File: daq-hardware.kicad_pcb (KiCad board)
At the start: 4 copper layers, 100 x 60 mm, 106 parts, among them J1 USB_B, J10 Screw_Terminal_01x02, J11 Screw_Terminal_01x01, J12 Screw_Terminal_01x01, J13 Screw_Terminal_01x01, J14 Screw_Terminal_01x01, J15 Barrel_Jack_Switch, J2 Micro_SD_Card_Det_Hirose_DM3AT, J3 Conn_01x02, J4 Screw_Terminal_01x02, J5 Screw_Terminal_Thermo_1, J6 Screw_Terminal_Thermo_2, J7 Screw_Terminal_Thermo_3, J8 Screw_Terminal_Thermo_4, J9 Screw_Terminal_01x02, Q1 MMDT2222A, Q2 PMV20ENR, Q3 PMV20ENR, SW1 SW1, SW2 SW1, U1 CP2102N-A01-GQFN24, U10 LTV-817S, U11 ADS131M04, U13 TPS2412PW, U2 ESP32-WROOM-32D, U3 TPS61093, U4 TPS62160DGK, U5 TPS62160DGK, U6 MAX31855RASA, U7 MAX31855RASA, U8 MAX31855RASA, U9 MAX31855RASA

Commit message: Added 3D models, added ptaps sheet, fixed pyros
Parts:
- added D7: CONTINUITY, LED_SMD:LED_0805_2012Metric, F.Cu at (286.4, 116.0)
- added J16: Conn_01x03, Connector_JST:JST_XH_B03B-XH-AM_1x03_P2.50mm_Vertical, F.Cu at (254.9, 117.9)
- added J17: Conn_01x03, Connector_JST:JST_XH_B03B-XH-AM_1x03_P2.50mm_Vertical, F.Cu at (254.9, 125.7)
- added J18: Conn_01x03, Connector_JST:JST_XH_B03B-XH-AM_1x03_P2.50mm_Vertical, F.Cu at (266.8, 117.9)
- added R29: 470, Resistor_SMD:R_0603_1608Metric, F.Cu at (290.6, 115.7)
- added R30: 22k, Resistor_SMD:R_0603_1608Metric, F.Cu at (265.4, 123.5)
- added R31: 43k, Resistor_SMD:R_0603_1608Metric, F.Cu at (277.3, 115.7)
- added R32: 22k, Resistor_SMD:R_0603_1608Metric, F.Cu at (269.4, 123.5)
- added R33: 43k, Resistor_SMD:R_0603_1608Metric, F.Cu at (265.4, 126.0)
- added R34: 22k, Resistor_SMD:R_0603_1608Metric, F.Cu at (277.3, 118.2)
- added R35: 43k, Resistor_SMD:R_0603_1608Metric, F.Cu at (269.4, 126.0)
- D4: value DIODE -> D_Schottky; footprint Diode_SMD:D_SMA -> Diode_SMD:D_SOD-123F
- R2: value 22k1 -> 22k
- R25: value 1k -> 470
- R3: value 47k5 -> 43k
- moved SW1 22.0 mm to (223.0, 152.0)
- moved U11 2.51 mm to (212.6, 52.3)
- moved D4 0.71 mm to (265.8, 87.8), turned to 90 degrees
- turned U10 to 180 degrees
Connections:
- J10 pad 2: Net-(D4-Pad1) -> Net-(D4-Pad2)
- Q2 pad 3: Net-(D4-Pad2) -> Net-(D4-Pad1)
- R25 pad 2: Net-(D4-Pad2) -> Net-(D4-Pad1)
- R26 pad 1: /pyro/CONT -> /CONT
- U10 pad 1: +3V3 -> Net-(D4-Pad2)
- U10 pad 2: /pyro/CONT -> Net-(R27-Pad1)
- U10 pad 3: Net-(R27-Pad1) -> /CONT
- U10 pad 4: Net-(D4-Pad1) -> +3V3
- U2 pad 36: (no net) -> /CONT
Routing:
- net Net-(D4-Pad2): track 17.7 -> 6.17 mm, vias 0 -> 1
- net Net-(D4-Pad1): track 7.27 -> 16.1 mm, vias 1 -> 0
- net +3V3: track 33.8 -> 27.3 mm
- net /pyro/CONT: track 3.93 -> 0.00 mm
- net Net-(R27-Pad1): track 7.31 -> 9.81 mm
- net Net-(Q3-Pad1): track 8.04 -> 7.11 mm
- net /MISO: track 58.3 -> 57.4 mm
- net GND: vias 274 -> 290
- net (no net): vias 14 -> 10

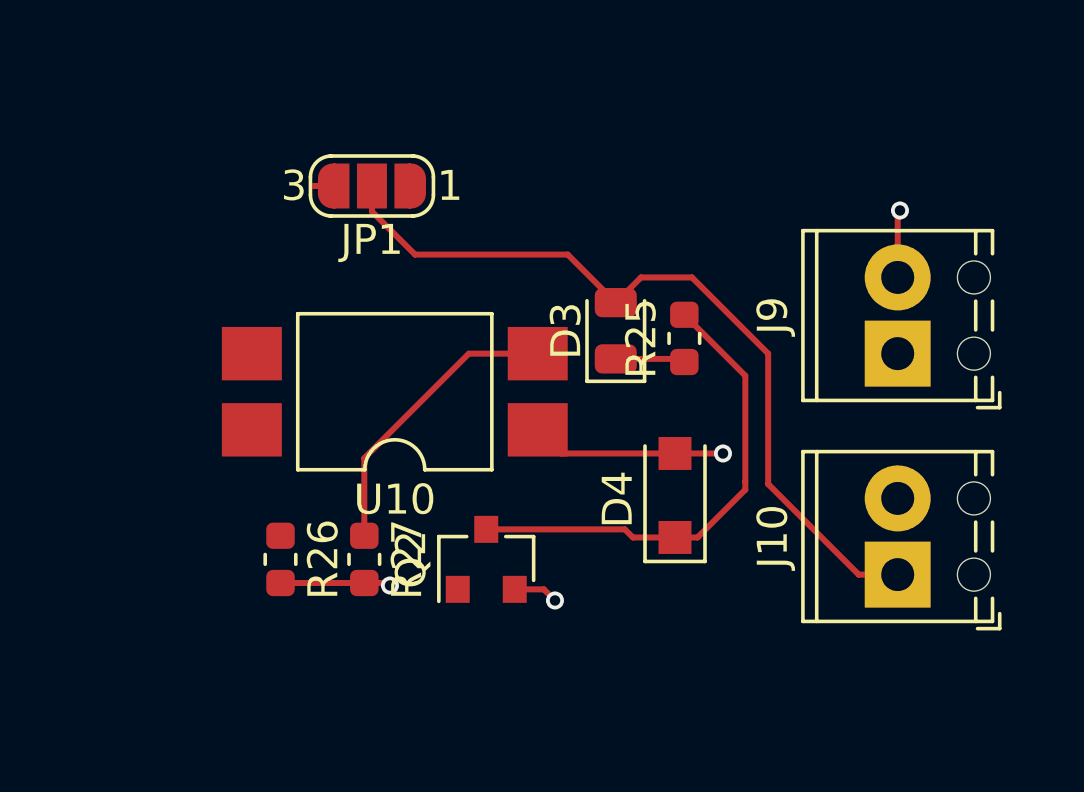
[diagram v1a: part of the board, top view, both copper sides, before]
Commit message: Minor PCB rerouting
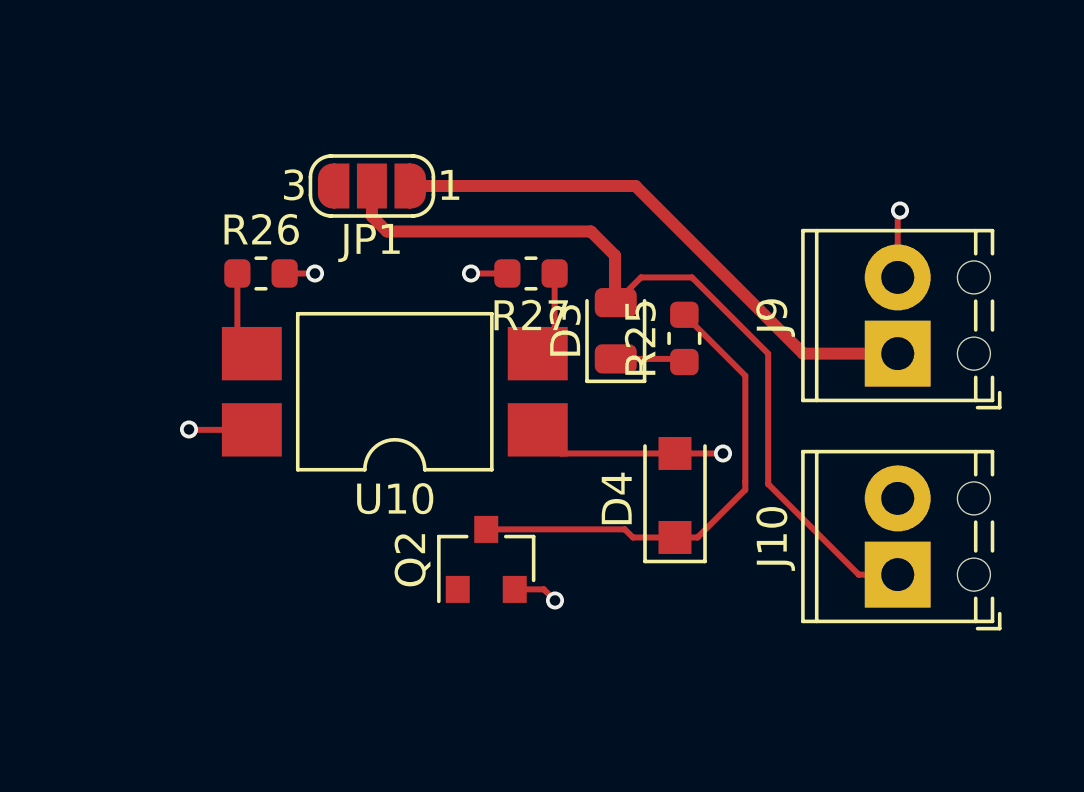
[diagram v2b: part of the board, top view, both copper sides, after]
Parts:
- moved R27 11.0 mm to (261.0, 80.4), turned to 180 degrees
- moved R26 9.55 mm to (252.0, 80.4), turned to 0 degrees
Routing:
- net Net-(J9-Pad1): track 0.00 -> 18.5 mm
- net Net-(R27-Pad1): track 9.81 -> 2.90 mm
- net /CONT: track 0.11 -> 2.98 mm
- net GND: track 35.5 -> 34.1 mm, vias 290 -> 291
- net +3V3: track 27.3 -> 28.7 mm, vias 7 -> 8
- net Net-(D3-Pad2): track 27.0 -> 28.0 mm
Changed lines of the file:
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@@
     (thickness 1.6)
     (drawings 14)
-    (tracks 680)
+    (tracks 689)
     (zones 0)
     (modules 117)
@@
   )
   (setup
-    (last_trace_width 0.4)
+    (last_trace_width 0.2)
     (user_trace_width 0.4)
     (trace_clearance 0.127)
@@
   )
   (module Resistor_SMD:R_0603_1608Metric (layer F.Cu)
-    (at 255.444 89.93 270)
+    (at 261 80.4 180)
     (descr "Resistor SMD 0603 (1608 Metric), square (rectangular) end terminal, IPC_7351 nominal, (Body size source: http://www.tortai-tech.com/upload/download/2011102023233369053.pdf), generated with kicad-footprint-generator")
     (tags resistor)
     (attr smd)
-    (fp_text reference R27 (at 0 -1.43 90) (layer F.SilkS)
+    (fp_text reference R27 (at 0 -1.43) (layer F.SilkS)
       (effects (font (size 1 1) (thickness 0.15)))
     )
-    (fp_text value 500 (at 0 1.43 90) (layer F.Fab)
+    (fp_text value 500 (at 0 1.43) (layer F.Fab)
       (effects (font (size 1 1) (thickness 0.15)))
     )
-    (fp_text user %R (at 0 0 90) (layer F.Fab)
+    (fp_text user %R (at 0 0) (layer F.Fab)
       (effects (font (size 0.4 0.4) (thickness 0.06)))
     )
@@
     (fp_line (start -0.8 -0.4) (end 0.8 -0.4) (layer F.Fab) (width 0.1))
     (fp_line (start -0.8 0.4) (end -0.8 -0.4) (layer F.Fab) (width 0.1))
-    (pad 2 smd roundrect (at 0.7875 0 270) (size 0.875 0.95) (layers F.Cu F.Paste F.Mask) (roundrect_rratio 0.25)
+    (pad 2 smd roundrect (at 0.7875 0 180) (size 0.875 0.95) (layers F.Cu F.Paste F.Mask) (roundrect_rratio 0.25)
       (net 1 GND))
-    (pad 1 smd roundrect (at -0.7875 0 270) (size 0.875 0.95) (layers F.Cu F.Paste F.Mask) (roundrect_rratio 0.25)
+    (pad 1 smd roundrect (at -0.7875 0 180) (size 0.875 0.95) (layers F.Cu F.Paste F.Mask) (roundrect_rratio 0.25)
       (net 66 "Net-(R27-Pad1)"))
     (model ${KISYS3DMOD}/Resistor_SMD.3dshapes/R_0603_1608Metric.wrl
@@
   )
   (module Resistor_SMD:R_0603_1608Metric (layer F.Cu)
-    (at 252.65 89.93 270)
+    (at 252 80.4)
     (descr "Resistor SMD 0603 (1608 Metric), square (rectangular) end terminal, IPC_7351 nominal, (Body size source: http://www.tortai-tech.com/upload/download/2011102023233369053.pdf), generated with kicad-footprint-generator")
     (tags resistor)
     (attr smd)
-    (fp_text reference R26 (at 0 -1.43 90) (layer F.SilkS)
+    (fp_text reference R26 (at 0 -1.43) (layer F.SilkS)
       (effects (font (size 1 1) (thickness 0.15)))
     )
-    (fp_text value 500 (at 0 1.43 90) (layer F.Fab)
+    (fp_text value 500 (at 0 1.43) (layer F.Fab)
       (effects (font (size 1 1) (thickness 0.15)))
     )
-    (fp_text user %R (at 0 0 90) (layer F.Fab)
+    (fp_text user %R (at 0 0) (layer F.Fab)
       (effects (font (size 0.4 0.4) (thickness 0.06)))
     )
@@
     (fp_line (start -0.8 -0.4) (end 0.8 -0.4) (layer F.Fab) (width 0.1))
     (fp_line (start -0.8 0.4) (end -0.8 -0.4) (layer F.Fab) (width 0.1))
-    (pad 2 smd roundrect (at 0.7875 0 270) (size 0.875 0.95) (layers F.Cu F.Paste F.Mask) (roundrect_rratio 0.25)
+    (pad 2 smd roundrect (at 0.7875 0) (size 0.875 0.95) (layers F.Cu F.Paste F.Mask) (roundrect_rratio 0.25)
       (net 1 GND))
-    (pad 1 smd roundrect (at -0.7875 0 270) (size 0.875 0.95) (layers F.Cu F.Paste F.Mask) (roundrect_rratio 0.25)
+    (pad 1 smd roundrect (at -0.7875 0) (size 0.875 0.95) (layers F.Cu F.Paste F.Mask) (roundrect_rratio 0.25)
       (net 81 /CONT))
     (model ${KISYS3DMOD}/Resistor_SMD.3dshapes/R_0603_1608Metric.wrl
@@
   (via (at 107.5 80.5) (size 0.6) (drill 0.35) (layers F.Cu B.Cu) (net 1))
   (via (at 199.5 132.5) (size 0.6) (drill 0.35) (layers F.Cu B.Cu) (net 1))
-  (segment (start 252.65 90.7175) (end 255.444 90.7175) (width 0.2) (layer F.Cu) (net 1) (status 30))
   (segment (start 260.458 90.93) (end 260.458 90.98) (width 0.2) (layer F.Cu) (net 1) (status 30))
   (via (at 108 139.5) (size 0.6) (drill 0.35) (layers F.Cu B.Cu) (net 1))
@@
   (segment (start 106.75 96.75) (end 107.9375 96.75) (width 0.2) (layer F.Cu) (net 1) (status 30))
   (segment (start 124.27 80.73) (end 124.5 80.5) (width 0.2) (layer B.Cu) (net 1))
-  (via (at 256.3 90.8) (size 0.6) (drill 0.35) (layers F.Cu B.Cu) (net 1))
-  (segment (start 256.2175 90.7175) (end 256.3 90.8) (width 0.2) (layer F.Cu) (net 1))
-  (segment (start 255.444 90.7175) (end 256.2175 90.7175) (width 0.2) (layer F.Cu) (net 1) (status 10))
   (via (at 261.8 91.3) (size 0.6) (drill 0.35) (layers F.Cu B.Cu) (net 1))
   (segment (start 261.43 90.93) (end 261.8 91.3) (width 0.2) (layer F.Cu) (net 1))
@@
   (via (at 148 103) (size 0.6) (drill 0.35) (layers F.Cu B.Cu) (net 1))
   (via (at 146.6 102) (size 0.6) (drill 0.35) (layers F.Cu B.Cu) (net 1))
+  (via (at 253.8 80.4) (size 0.6) (drill 0.35) (layers F.Cu B.Cu) (net 1))
+  (segment (start 252.7875 80.4) (end 253.8 80.4) (width 0.2) (layer F.Cu) (net 1))
+  (via (at 259 80.4) (size 0.6) (drill 0.35) (layers F.Cu B.Cu) (net 1))
+  (segment (start 260.2125 80.4) (end 259 80.4) (width 0.2) (layer F.Cu) (net 1))
   (segment (start 118.6 87.8) (end 118.6 89.5) (width 0.2) (layer F.Cu) (net 2))
   (segment (start 117.3 86.5) (end 118.6 87.8) (width 0.2) (layer F.Cu) (net 2) (status 10))
@@
   (segment (start 134.4 100.6125) (end 134.9875 100.6125) (width 0.4) (layer F.Cu) (net 4))
   (segment (start 134.9875 100.6125) (end 135.5 100.1) (width 0.4) (layer F.Cu) (net 4))
-  (segment (start 253.698 77.484) (end 254.398 77.484) (width 0.2) (layer F.Cu) (net 4))
+  (via (at 249.6 85.6) (size 0.6) (drill 0.35) (layers F.Cu B.Cu) (net 4))
+  (segment (start 251.695 85.612) (end 249.612 85.612) (width 0.2) (layer F.Cu) (net 4))
+  (segment (start 249.612 85.612) (end 249.6 85.6) (width 0.2) (layer F.Cu) (net 4))
   (segment (start 114.89799 95.409108) (end 116.307098 94) (width 0.2) (layer F.Cu) (net 5))
   (segment (start 115.6 97.3875) (end 114.89799 96.68549) (width 0.2) (layer F.Cu) (net 5) (status 10))
@@
   (segment (start 268.906 87.42) (end 271.924 90.438) (width 0.2) (layer F.Cu) (net 36))
   (segment (start 263.826 81.3725) (end 264.6665 80.532) (width 0.2) (layer F.Cu) (net 36) (status 10))
-  (segment (start 262.2235 79.77) (end 263.826 81.3725) (width 0.2) (layer F.Cu) (net 36) (status 20))
-  (segment (start 257.134 79.77) (end 262.2235 79.77) (width 0.2) (layer F.Cu) (net 36))
-  (segment (start 255.698 77.484) (end 255.698 78.334) (width 0.2) (layer F.Cu) (net 36) (status 10))
-  (segment (start 255.698 78.334) (end 257.134 79.77) (width 0.2) (layer F.Cu) (net 36))
+  (segment (start 263.8 81.3465) (end 263.826 81.3725) (width 0.4) (layer F.Cu) (net 36))
+  (segment (start 263.8 79.8) (end 263.8 81.3465) (width 0.4) (layer F.Cu) (net 36))
+  (segment (start 263 79) (end 263.8 79.8) (width 0.4) (layer F.Cu) (net 36))
+  (segment (start 256.2 79) (end 263 79) (width 0.4) (layer F.Cu) (net 36))
+  (segment (start 255.698 77.484) (end 255.698 78.498) (width 0.4) (layer F.Cu) (net 36))
+  (segment (start 255.698 78.498) (end 256.2 79) (width 0.4) (layer F.Cu) (net 36))
   (segment (start 266.008 83.2475) (end 266.112 83.3515) (width 0.2) (layer F.Cu) (net 37) (status 30))
   (segment (start 263.826 83.2475) (end 266.008 83.2475) (width 0.2) (layer F.Cu) (net 37) (status 30))
@@
   (segment (start 128.3 90.7) (end 128.3 92.2) (width 0.4) (layer F.Cu) (net 57))
   (segment (start 118 84.6) (end 123 89.6) (width 0.4) (layer F.Cu) (net 57))
+  (segment (start 257.598 77.484) (end 256.998 77.484) (width 0.4) (layer F.Cu) (net 58))
+  (segment (start 264.484 77.484) (end 257.598 77.484) (width 0.4) (layer F.Cu) (net 58))
+  (segment (start 273.224 83.072) (end 270.072 83.072) (width 0.4) (layer F.Cu) (net 58))
+  (segment (start 270.072 83.072) (end 264.484 77.484) (width 0.4) (layer F.Cu) (net 58))
   (segment (start 134.3875 102.2) (end 134.4 102.1875) (width 0.2) (layer F.Cu) (net 64))
   (segment (start 132.9875 102.2) (end 134.3875 102.2) (width 0.2) (layer F.Cu) (net 64))
   (segment (start 132.4 101.6125) (end 132.9875 102.2) (width 0.2) (layer F.Cu) (net 64))
   (segment (start 132.4 100.575) (end 132.4 101.6125) (width 0.2) (layer F.Cu) (net 64))
-  (segment (start 258.928 83.072) (end 261.225 83.072) (width 0.2) (layer F.Cu) (net 66))
-  (segment (start 255.444 89.1425) (end 255.444 86.556) (width 0.2) (layer F.Cu) (net 66))
-  (segment (start 255.444 86.556) (end 258.928 83.072) (width 0.2) (layer F.Cu) (net 66))
+  (segment (start 261.7875 82.5095) (end 261.225 83.072) (width 0.2) (layer F.Cu) (net 66))
+  (segment (start 261.7875 80.4) (end 261.7875 82.5095) (width 0.2) (layer F.Cu) (net 66))
   (segment (start 130.55 91.55) (end 130.7 91.4) (width 0.4) (layer F.Cu) (net 73))
   (segment (start 130.55 93) (end 130.55 91.55) (width 0.4) (layer F.Cu) (net 73))
@@
   (segment (start 136.175 88.75) (end 136.175 91.525) (width 0.2) (layer F.Cu) (net 76))
   (segment (start 136.175 91.525) (end 134.7 93) (width 0.2) (layer F.Cu) (net 76))
+  (segment (start 251.2125 82.5895) (end 251.695 83.072) (width 0.2) (layer F.Cu) (net 81))
+  (segment (start 251.2125 80.4) (end 251.2125 82.5895) (width 0.2) (layer F.Cu) (net 81))
   (zone (net 1) (net_name GND) (layer In1.Cu) (hatch edge 0.508)
     (priority 1)

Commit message: layout changes
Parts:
- removed JP3: Jumper, Connector_PinHeader_2.54mm:PinHeader_1x02_P2.54mm_Vertical
- moved R29 160.4 mm to (130.3, 118.8), turned to 180 degrees
- moved D7 156.0 mm to (130.4, 116.2)
- moved R31 139.5 mm to (137.8, 116.2)
- moved R34 139.5 mm to (137.8, 118.8), turned to 180 degrees
- moved R32 135.7 mm to (134.0, 113.8), turned to 180 degrees
- moved R35 135.6 mm to (134.0, 118.8)
- moved SW2 132.8 mm to (104.2, 125.5), turned to 180 degrees
- moved C2 132.1 mm to (108.5, 121.2)
- moved R33 131.7 mm to (134.0, 116.2)
- moved R8 130.0 mm to (102.0, 122.0), turned to 270 degrees
- moved R7 128.1 mm to (104.5, 121.2)
- moved C3 128.0 mm to (104.5, 122.8)
- moved R30 127.9 mm to (137.8, 113.8), turned to 180 degrees
- moved R9 127.8 mm to (110.0, 99.8)
- moved J17 124.6 mm to (131.5, 108.2)
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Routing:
- net /PYRO: track 0.00 -> 85.4 mm, vias 0 -> 4
- net /CONT: track 2.98 -> 78.2 mm, vias 0 -> 4
- net /MOSI: track 0.00 -> 68.2 mm, vias 0 -> 2
- net Net-(D4-Pad2): track 6.17 -> 61.8 mm, vias 1 -> 3
- net /CLKOUT: track 0.00 -> 54.6 mm, vias 0 -> 2
- net /BOOT: track 9.17 -> 40.9 mm, vias 0 -> 2
- net GND: track 34.1 -> 64.8 mm, vias 291 -> 279
- net /RESET: track 31.1 -> 57.2 mm, vias 2 -> 3
- net /analogue/AIN3N: track 0.00 -> 18.5 mm
- net /analogue/AIN2N: track 0.00 -> 17.9 mm
- net /MISO: track 57.4 -> 73.1 mm, vias 4 -> 5
- net /analogue/AIN3P: track 0.00 -> 15.4 mm, vias 0 -> 1
- net /analogue/AIN0P: track 0.00 -> 15.3 mm
- net /SCLK: track 61.6 -> 76.9 mm
- net Net-(C2-Pad1): track 0.00 -> 14.8 mm
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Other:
- board text added: "yeet"

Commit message: Add Copper
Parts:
- moved U3 76.8 mm to (165.0, 97.0), turned to 90 degrees
- moved C6 76.4 mm to (164.0, 101.7), turned to 270 degrees
- moved L3 74.9 mm to (156.8, 92.3), turned to 90 degrees
- moved R20 70.0 mm to (153.8, 92.7), turned to 270 degrees
- moved R16 68.9 mm to (163.0, 92.0), turned to 90 degrees
- moved R22 68.3 mm to (159.5, 92.0), turned to 90 degrees
- moved R17 66.5 mm to (161.2, 92.0), turned to 90 degrees
- moved C8 63.6 mm to (168.2, 92.0), turned to 90 degrees
- moved C9 63.0 mm to (164.8, 92.0), turned to 270 degrees
- moved C7 62.2 mm to (165.8, 101.8), turned to 90 degrees
- moved C10 62.0 mm to (161.8, 96.5), turned to 270 degrees
- moved R24 60.0 mm to (159.8, 96.5), turned to 90 degrees
- moved U5 53.6 mm to (155.8, 98.0), turned to 90 degrees
- moved R18 53.5 mm to (166.5, 92.0), turned to 90 degrees
- moved C14 53.2 mm to (164.4, 84.7), turned to 90 degrees
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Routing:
- net /power/PG: track 2.66 -> 28.9 mm
- net GND: track 64.8 -> 85.1 mm, vias 279 -> 286
- net +3V3: track 43.1 -> 54.5 mm, vias 18 -> 21
- net Net-(R16-Pad2): track 0.00 -> 10.1 mm
- net Net-(L1-Pad2): track 0.00 -> 8.99 mm, vias 0 -> 2
- net Net-(R22-Pad1): track 0.00 -> 7.24 mm
- net Net-(C8-Pad1): track 0.00 -> 5.16 mm
- net +12V: track 0.00 -> 4.81 mm
- net Net-(C7-Pad1): track 0.00 -> 4.30 mm
- net Net-(L3-Pad1): track 0.00 -> 3.78 mm
- net +5V: track 0.00 -> 2.72 mm, vias 0 -> 4
- net /power/VO: track 0.00 -> 2.63 mm
- net Net-(C7-Pad2): track 0.00 -> 2.52 mm
- added copper zone on F.Cu, net +12V
- added copper zone on F.Cu, net +5V
- added copper zone on F.Cu, net /power/VO
- added copper zone on F.Cu, net Net-(C7-Pad1)
- added copper zone on F.Cu, net Net-(C7-Pad2)
- added copper zone on F.Cu, net Net-(L3-Pad1)
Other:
- board text added: "ICLR DAQ r0 Designed by: Yasmine Chan Iris Clercq-Roques Han Liangyu Luca Mazzotta Nicolo’ Marsucco Luis Marques Shreeyam Kacker"
